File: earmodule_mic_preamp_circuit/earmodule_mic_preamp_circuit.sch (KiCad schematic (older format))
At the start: 29 parts

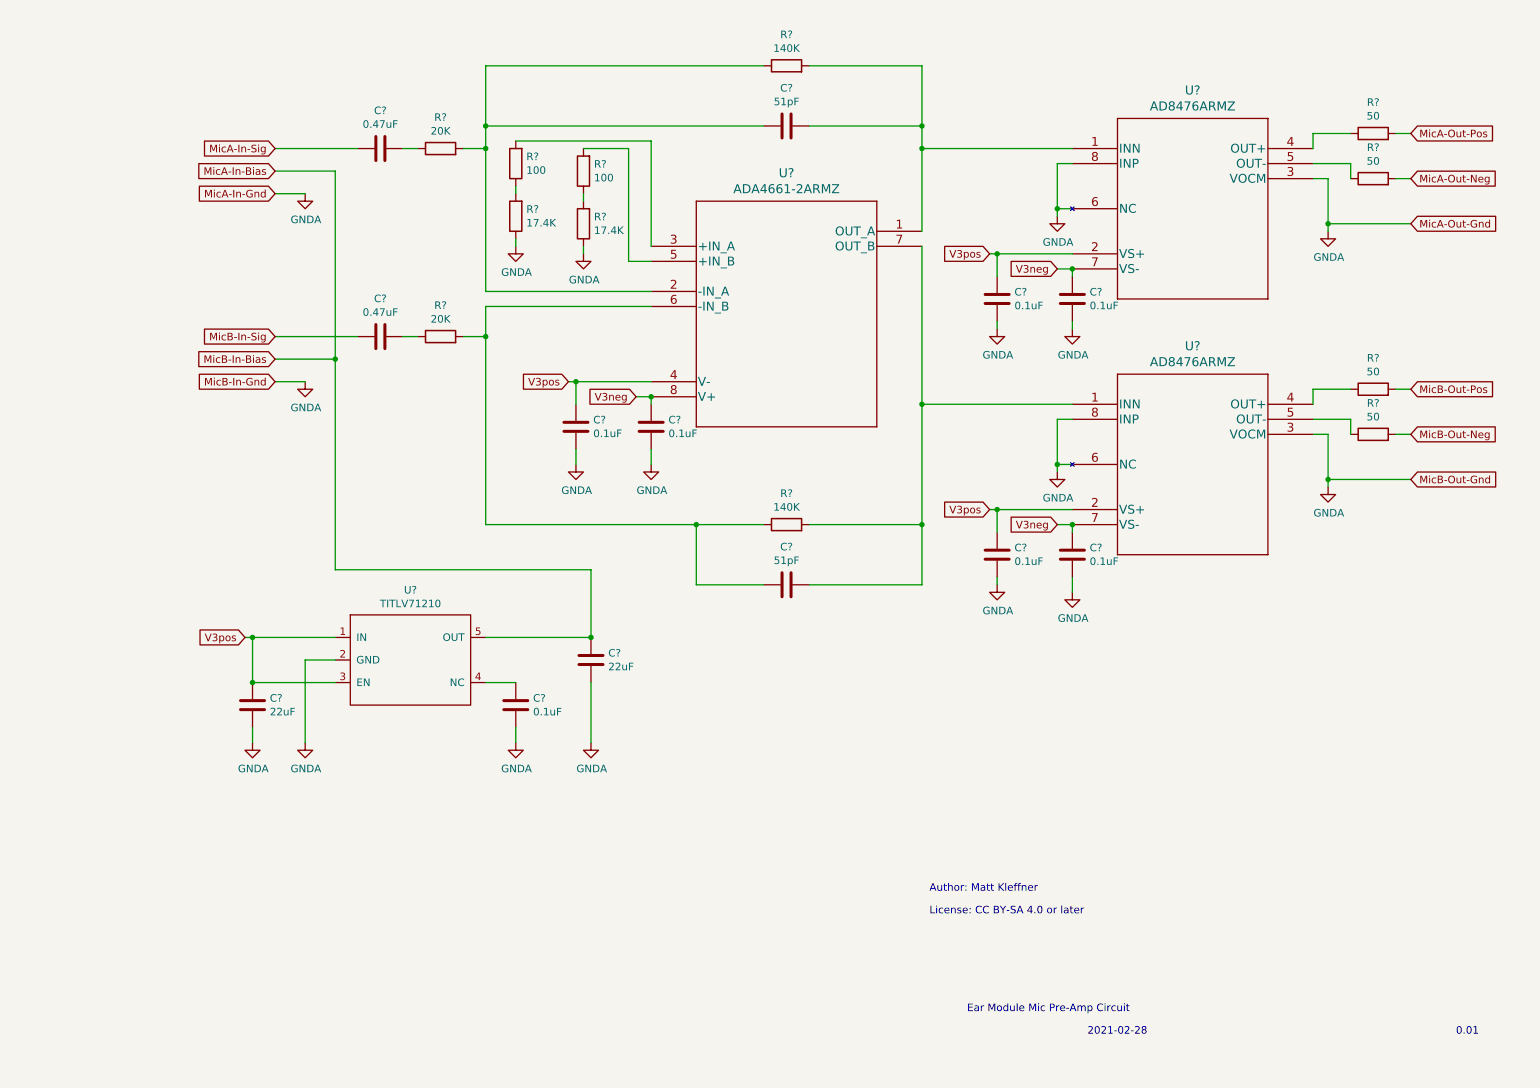
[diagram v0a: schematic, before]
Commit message: First complete PCB layout. Silkscreen needs to be fixed.
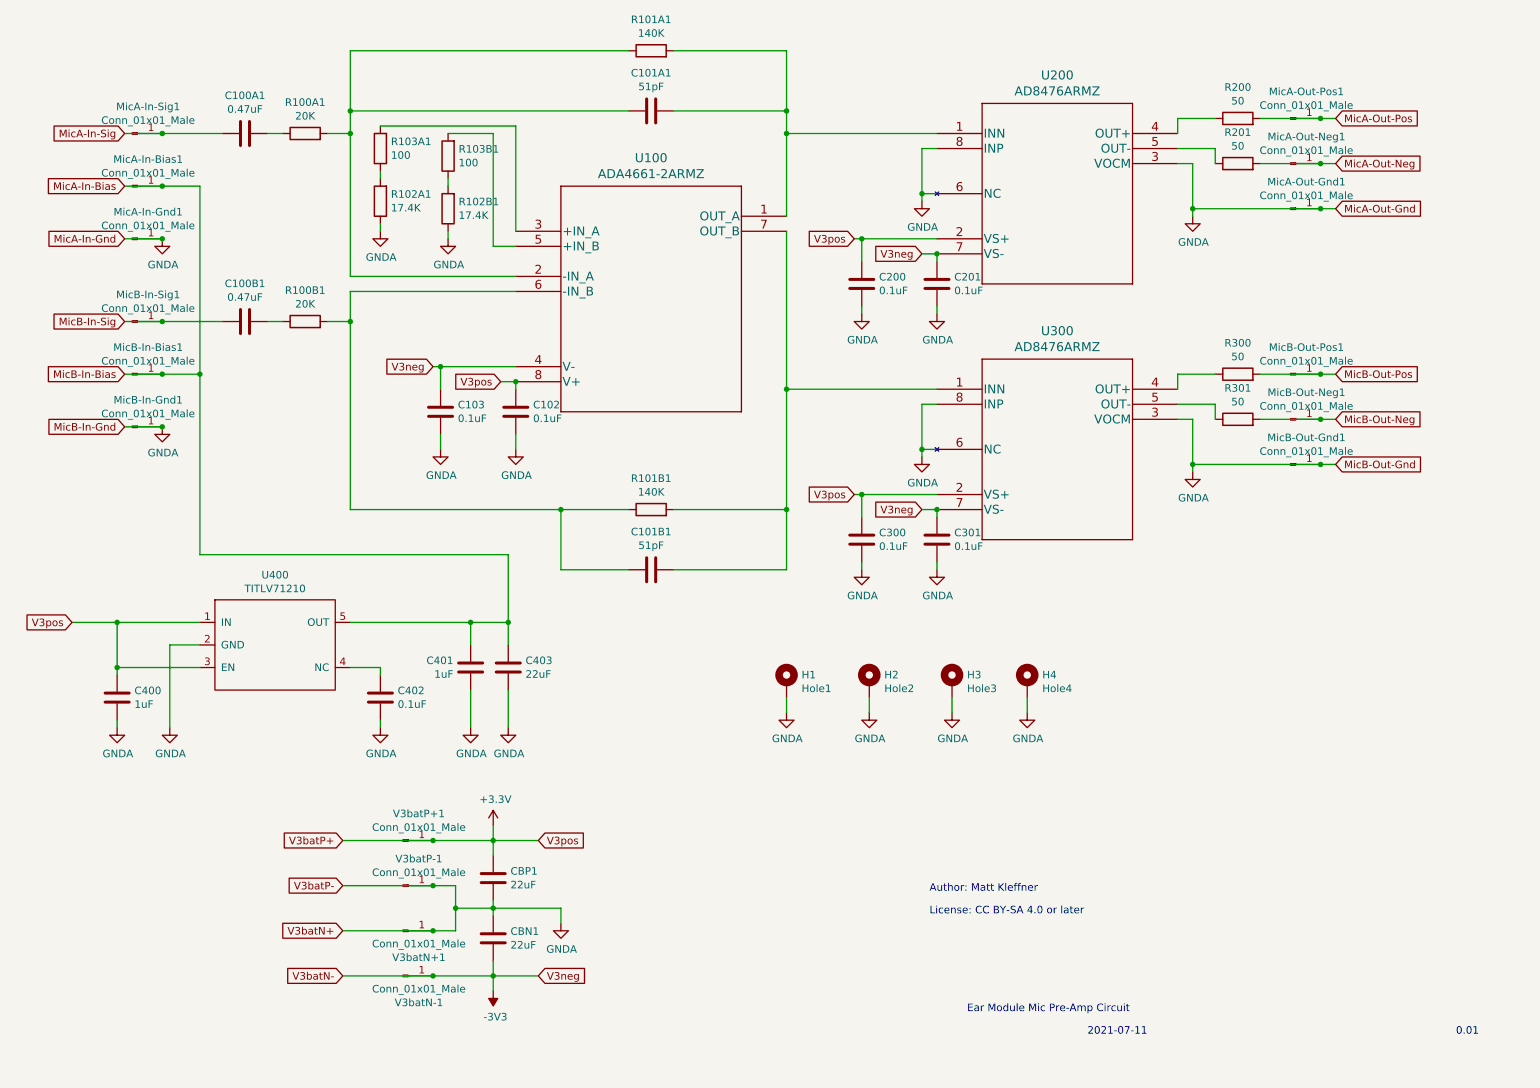
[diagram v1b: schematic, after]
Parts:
- added C400, C401: 1uF, Capacitor_SMD:C_0805_2012Metric_Pad1.15x1.40mm_HandSolder, symbol Device:C
- added CBN1: 22uF, Capacitor_SMD:C_1206_3216Metric_Pad1.42x1.75mm_HandSolder, symbol Device:C
- added H1: Hole1, MountingHole:MountingHole_2.7mm_M2.5_ISO7380, symbol Mechanical:MountingHole_Pad
- added H2: Hole2, MountingHole:MountingHole_2.7mm_M2.5_ISO7380, symbol Mechanical:MountingHole_Pad
- added H3: Hole3, MountingHole:MountingHole_2.7mm_M2.5_ISO7380, symbol Mechanical:MountingHole_Pad
- added H4: Hole4, MountingHole:MountingHole_2.7mm_M2.5_ISO7380, symbol Mechanical:MountingHole_Pad
- added MicA-In-Bias1, MicA-In-Gnd1, MicA-In-Sig1, MicA-Out-Gnd1, MicA-Out-Neg1, MicA-Out-Pos1, MicB-In-Bias1, MicB-In-Gnd1, MicB-In-Sig1, MicB-Out-Gnd1, MicB-Out-Neg1, MicB-Out-Pos1, V3batN+1, V3batN-1, V3batP+1, V3batP-1: Conn_01x01_Male, TestPoint:TestPoint_Pad_D2.0mm, symbol Connector:Conn_01x01_Male
- C100A1, C100B1, C101A1, C101B1, C102, C103, C200, C201, C300, C301, C402: renamed from C?; footprint (none) -> Capacitor_SMD:C_0402_1005Metric
- C403, CBP1: renamed from C?; footprint (none) -> Capacitor_SMD:C_1206_3216Metric_Pad1.42x1.75mm_HandSolder
- R100A1, R100B1, R101A1, R101B1, R102A1, R102B1, R103A1, R103B1, R200, R201, R300, R301: renamed from R?; footprint (none) -> Resistor_SMD:R_0402_1005Metric
- U100: renamed from U?; footprint RM_8_ADI -> footprints:ADA4661-2ARMZ
- U200, U300: renamed from U?; footprint RM_8_ADI -> footprints:AD8476ARMZ
- U400: renamed from U?; footprint (none) -> Package_TO_SOT_SMD:SOT-23-5_HandSoldering
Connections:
- net GNDA: now also C400.2, C401.2, CBN1.1, H1.1, H2.1, H3.1, H4.1, MicA-In-Gnd1.1 (Pin_1), MicA-Out-Gnd1.1 (Pin_1), MicB-In-Gnd1.1 (Pin_1), MicB-Out-Gnd1.1 (Pin_1), V3batN+1.1 (Pin_1), V3batP-1.1 (Pin_1)
- net MicA-In-Bias: now also C401.1, MicA-In-Bias1.1 (Pin_1), MicB-In-Bias1.1 (Pin_1)
- net MicA-In-Sig: now also MicA-In-Sig1.1 (Pin_1)
- net MicA-Out-Neg: now also MicA-Out-Neg1.1 (Pin_1)
- net MicA-Out-Pos: now also MicA-Out-Pos1.1 (Pin_1)
- net MicB-In-Sig: now also MicB-In-Sig1.1 (Pin_1)
- net MicB-Out-Neg: now also MicB-Out-Neg1.1 (Pin_1)
- net MicB-Out-Pos: now also MicB-Out-Pos1.1 (Pin_1)
- net V3neg renamed -3V3
- net -3V3: now also C103.1, U100.4 (V-), CBN1.2, V3batN-1.1 (Pin_1); no longer C102.1, U100.8 (V+)
- net V3pos renamed +3V3
- net +3V3: now also C102.1, U100.8 (V+), C400.1, V3batP+1.1 (Pin_1); no longer C103.1, U100.4 (V-)
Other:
- note added: "2021-07-11"
- note removed: "2021-02-28"
- moved on the sheet: C100A1, C100B1, C101A1, C101B1, C102, C103, C200, C201, C300, C301, C402, C403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

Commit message: Rearranged regulator layout for better co-location of parts. Cleaned up interface names.
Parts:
- renumbered MicA-In-Bias1 to MicInA-Bias1, MicA-In-Gnd1 to MicInA-Gnd1, MicA-In-Sig1 to MicInA-Sig1, MicB-In-Bias1 to MicInB-Bias1, MicB-In-Gnd1 to MicInB-Gnd1, MicB-In-Sig1 to MicInB-Sig1, MicA-Out-Gnd1 to MicOutA-Gnd1, MicA-Out-Neg1 to MicOutA-Neg1, MicA-Out-Pos1 to MicOutA-Pos1, MicB-Out-Gnd1 to MicOutB-Gnd1, MicB-Out-Neg1 to MicOutB-Neg1, MicB-Out-Pos1 to MicOutB-Pos1
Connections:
- net MicA-In-Bias renamed MicInA-Bias
- net MicA-In-Sig renamed MicInA-Sig
- net MicA-Out-Neg renamed MicOutA-Neg
- net MicA-Out-Pos renamed MicOutA-Pos
- net MicB-In-Sig renamed MicInB-Sig
- net MicB-Out-Neg renamed MicOutB-Neg
- net MicB-Out-Pos renamed MicOutB-Pos
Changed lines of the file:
@@
 	1800 1650 2050 1650
 $Comp
-L Connector:Conn_01x01_Male MicA-In-Sig1
+L Connector:Conn_01x01_Male MicInA-Sig1
 U 1 1 60ED7398
 P 1850 1650
-F 0 "MicA-In-Sig1" H 1956 1828 50  0000 C CNN
+F 0 "MicInA-Sig1" H 1956 1828 50  0000 C CNN
 F 1 "Conn_01x01_Male" H 1956 1737 50  0000 C CNN
 F 2 "TestPoint:TestPoint_Pad_D2.0mm" H 1850 1650 50  0001 C CNN
@@
 $EndComp
 $Comp
-L Connector:Conn_01x01_Male MicA-In-Bias1
+L Connector:Conn_01x01_Male MicInA-Bias1
 U 1 1 60EDA311
 P 1850 2000
-F 0 "MicA-In-Bias1" H 1956 2178 50  0000 C CNN
+F 0 "MicInA-Bias1" H 1956 2178 50  0000 C CNN
 F 1 "Conn_01x01_Male" H 1956 2087 50  0000 C CNN
 F 2 "TestPoint:TestPoint_Pad_D2.0mm" H 1850 2000 50  0001 C CNN
@@
 $EndComp
 $Comp
-L Connector:Conn_01x01_Male MicA-In-Gnd1
+L Connector:Conn_01x01_Male MicInA-Gnd1
 U 1 1 60EDDFEE
 P 1850 2350
-F 0 "MicA-In-Gnd1" H 1956 2528 50  0000 C CNN
+F 0 "MicInA-Gnd1" H 1956 2528 50  0000 C CNN
 F 1 "Conn_01x01_Male" H 1956 2437 50  0000 C CNN
 F 2 "TestPoint:TestPoint_Pad_D2.0mm" H 1850 2350 50  0001 C CNN
@@
 	2300 2000 2300 3250
 $Comp
-L Connector:Conn_01x01_Male MicB-In-Sig1
+L Connector:Conn_01x01_Male MicInB-Sig1
 U 1 1 60F3507A
 P 1850 2900
-F 0 "MicB-In-Sig1" H 1956 3078 50  0000 C CNN
+F 0 "MicInB-Sig1" H 1956 3078 50  0000 C CNN
 F 1 "Conn_01x01_Male" H 1956 2987 50  0000 C CNN
 F 2 "TestPoint:TestPoint_Pad_D2.0mm" H 1850 2900 50  0001 C CNN
@@
 $EndComp
 $Comp
-L Connector:Conn_01x01_Male MicB-In-Bias1
+L Connector:Conn_01x01_Male MicInB-Bias1
 U 1 1 60F390E4
 P 1850 3250
-F 0 "MicB-In-Bias1" H 1956 3428 50  0000 C CNN
+F 0 "MicInB-Bias1" H 1956 3428 50  0000 C CNN
 F 1 "Conn_01x01_Male" H 1956 3337 50  0000 C CNN
 F 2 "TestPoint:TestPoint_Pad_D2.0mm" H 1850 3250 50  0001 C CNN
@@
 $EndComp
 $Comp
-L Connector:Conn_01x01_Male MicB-In-Gnd1
+L Connector:Conn_01x01_Male MicInB-Gnd1
 U 1 1 60F3D199
 P 1850 3600
-F 0 "MicB-In-Gnd1" H 1956 3778 50  0000 C CNN
+F 0 "MicInB-Gnd1" H 1956 3778 50  0000 C CNN
 F 1 "Conn_01x01_Male" H 1956 3687 50  0000 C CNN
 F 2 "TestPoint:TestPoint_Pad_D2.0mm" H 1850 3600 50  0001 C CNN
@@
 	8900 2150 8900 2200
 $Comp
-L Connector:Conn_01x01_Male MicA-Out-Pos1
+L Connector:Conn_01x01_Male MicOutA-Pos1
 U 1 1 60FA54FA
 P 9550 1550
-F 0 "MicA-Out-Pos1" H 9656 1728 50  0000 C CNN
+F 0 "MicOutA-Pos1" H 9656 1728 50  0000 C CNN
 F 1 "Conn_01x01_Male" H 9656 1637 50  0000 C CNN
 F 2 "TestPoint:TestPoint_Pad_D2.0mm" H 9550 1550 50  0001 C CNN
@@
 	9350 1550 9750 1550
 $Comp
-L Connector:Conn_01x01_Male MicA-Out-Neg1
+L Connector:Conn_01x01_Male MicOutA-Neg1
 U 1 1 60FAAA8C
 P 9550 1850
-F 0 "MicA-Out-Neg1" H 9656 2028 50  0000 C CNN
+F 0 "MicOutA-Neg1" H 9656 2028 50  0000 C CNN
 F 1 "Conn_01x01_Male" H 9656 1937 50  0000 C CNN
 F 2 "TestPoint:TestPoint_Pad_D2.0mm" H 9550 1850 50  0001 C CNN
@@
 $EndComp
 $Comp
-L Connector:Conn_01x01_Male MicA-Out-Gnd1
+L Connector:Conn_01x01_Male MicOutA-Gnd1
 U 1 1 60FAEA59
 P 9550 2150
-F 0 "MicA-Out-Gnd1" H 9656 2328 50  0000 C CNN
+F 0 "MicOutA-Gnd1" H 9656 2328 50  0000 C CNN
 F 1 "Conn_01x01_Male" H 9656 2237 50  0000 C CNN
 F 2 "TestPoint:TestPoint_Pad_D2.0mm" H 9550 2150 50  0001 C CNN
@@
 	7200 2050 7100 2050
 $Comp
-L Connector:Conn_01x01_Male MicB-Out-Pos1
+L Connector:Conn_01x01_Male MicOutB-Pos1
 U 1 1 60FBFF69
 P 9550 3250
-F 0 "MicB-Out-Pos1" H 9656 3428 50  0000 C CNN
+F 0 "MicOutB-Pos1" H 9656 3428 50  0000 C CNN
 F 1 "Conn_01x01_Male" H 9656 3337 50  0000 C CNN
 F 2 "TestPoint:TestPoint_Pad_D2.0mm" H 9550 3250 50  0001 C CNN
@@
 	8900 3850 8900 3900
 $Comp
-L Connector:Conn_01x01_Male MicB-Out-Neg1
+L Connector:Conn_01x01_Male MicOutB-Neg1
 U 1 1 60FDC45F
 P 9550 3550
-F 0 "MicB-Out-Neg1" H 9656 3728 50  0000 C CNN
+F 0 "MicOutB-Neg1" H 9656 3728 50  0000 C CNN
 F 1 "Conn_01x01_Male" H 9656 3637 50  0000 C CNN
 F 2 "TestPoint:TestPoint_Pad_D2.0mm" H 9550 3550 50  0001 C CNN
@@
 	9750 3250 9850 3250
 $Comp
-L Connector:Conn_01x01_Male MicB-Out-Gnd1
+L Connector:Conn_01x01_Male MicOutB-Gnd1
 U 1 1 60FE4399
 P 9550 3850
-F 0 "MicB-Out-Gnd1" H 9656 4028 50  0000 C CNN
+F 0 "MicOutB-Gnd1" H 9656 4028 50  0000 C CNN
 F 1 "Conn_01x01_Male" H 9656 3937 50  0000 C CNN
 F 2 "TestPoint:TestPoint_Pad_D2.0mm" H 9550 3850 50  0001 C CNN
@@
 Wire Wire Line
 	4000 6650 3850 6650
-Wire Wire Line
-	3250 6950 3850 6950
-Wire Wire Line
-	3250 7250 3850 7250
-Connection ~ 3850 6350
-Wire Wire Line
-	3850 6350 3250 6350
 $Comp
 L Connector:Conn_01x01_Male V3batP-1
@@
 	1    0    0    1
 $EndComp
-Connection ~ 3850 6650
-Wire Wire Line
-	3850 6650 3250 6650
-Connection ~ 3850 7250
 Wire Wire Line
 	3850 6350 4250 6350
@@
 Text GLabel 4550 7250 2    50   Input ~ 0
 V3neg
-Connection ~ 3850 6950
 Wire Wire Line
 	3850 6950 4000 6950
@@
 Wire Wire Line
 	4250 7250 4550 7250
-Text GLabel 3250 7250 0    50   Input ~ 0
-V3batN-
-Text GLabel 3250 6950 0    50   Input ~ 0
-V3batN+
-Text GLabel 3250 6650 0    50   Input ~ 0
-V3batP-
-Text GLabel 3250 6350 0    50   Input ~ 0
-V3batP+
 Text GLabel 9850 3250 2    50   Input ~ 0
-MicB-Out-Pos
+MicOutB-Pos
 Text GLabel 9850 3550 2    50   Input ~ 0
-MicB-Out-Neg
+MicOutB-Neg
 Text GLabel 9850 3850 2    50   Input ~ 0
-MicB-Out-Gnd
+MicOutB-Gnd
 Text GLabel 9850 1550 2    50   Input ~ 0
-MicA-Out-Pos
+MicOutA-Pos
 Text GLabel 9850 1850 2    50   Input ~ 0
-MicA-Out-Neg
+MicOutA-Neg
 Text GLabel 9850 2150 2    50   Input ~ 0
-MicA-Out-Gnd
+MicOutA-Gnd
 Text GLabel 1800 1650 0    50   Input ~ 0
-MicA-In-Sig
+MicInA-Sig
 Text GLabel 1800 2900 0    50   Input ~ 0
-MicB-In-Sig
+MicInB-Sig
 Text GLabel 1800 3600 0    50   Input ~ 0
-MicB-In-Gnd
+MicInB-Gnd
 Text GLabel 1800 2350 0    50   Input ~ 0
-MicA-In-Gnd
+MicInA-Gnd
 Text GLabel 1800 3250 0    50   Input ~ 0
-MicB-In-Bias
+MicInB-Bias
 Text GLabel 1800 2000 0    50   Input ~ 0
-MicA-In-Bias
+MicInA-Bias
 $Comp
 L Mechanical:MountingHole_Pad H1

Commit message: Enlarged board and wire solder pad sizes. Added small decoupling caps in bias circuit. Finalized naming, numbering, and placement of text.
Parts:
- removed H1: Hole1, MountingHole:MountingHole_2.7mm_M2.5_ISO7380, symbol Mechanical:MountingHole_Pad
- removed H2: Hole2, MountingHole:MountingHole_2.7mm_M2.5_ISO7380, symbol Mechanical:MountingHole_Pad
- removed H3: Hole3, MountingHole:MountingHole_2.7mm_M2.5_ISO7380, symbol Mechanical:MountingHole_Pad
- removed H4: Hole4, MountingHole:MountingHole_2.7mm_M2.5_ISO7380, symbol Mechanical:MountingHole_Pad
- added C401: 0.1uF, Capacitor_SMD:C_0402_1005Metric, symbol Device:C
- added H1, H2, H3, H4: MountingHole, MountingHole:MountingHole_2.7mm_M2.5_ISO7380, symbol Mechanical:MountingHole
- MicIn-Bias1: renamed from MicInA-Bias1; footprint TestPoint:TestPoint_Pad_D2.0mm -> TestPoint:TestPoint_Pad_D4.0mm
- MicIn-Bias2: renamed from MicInB-Bias1; footprint TestPoint:TestPoint_Pad_D2.0mm -> TestPoint:TestPoint_Pad_D4.0mm
- MicIn-Gnd1: renamed from MicInA-Gnd1; footprint TestPoint:TestPoint_Pad_D2.0mm -> TestPoint:TestPoint_Pad_D4.0mm
- MicIn-Gnd2: renamed from MicInB-Gnd1; footprint TestPoint:TestPoint_Pad_D2.0mm -> TestPoint:TestPoint_Pad_D4.0mm
- MicIn-Sig1: renamed from MicInA-Sig1; footprint TestPoint:TestPoint_Pad_D2.0mm -> TestPoint:TestPoint_Pad_D4.0mm
- MicIn-Sig2: renamed from MicInB-Sig1; footprint TestPoint:TestPoint_Pad_D2.0mm -> TestPoint:TestPoint_Pad_D4.0mm
- MicOut-Gnd1: renamed from MicOutA-Gnd1; footprint TestPoint:TestPoint_Pad_D2.0mm -> TestPoint:TestPoint_Pad_D4.0mm
- MicOut-Gnd2: renamed from MicOutB-Gnd1; footprint TestPoint:TestPoint_Pad_D2.0mm -> TestPoint:TestPoint_Pad_D4.0mm
- MicOut-Neg1: renamed from MicOutA-Neg1; footprint TestPoint:TestPoint_Pad_D2.0mm -> TestPoint:TestPoint_Pad_D4.0mm
- MicOut-Neg2: renamed from MicOutB-Neg1; footprint TestPoint:TestPoint_Pad_D2.0mm -> TestPoint:TestPoint_Pad_D4.0mm
- MicOut-Pos1: renamed from MicOutA-Pos1; footprint TestPoint:TestPoint_Pad_D2.0mm -> TestPoint:TestPoint_Pad_D4.0mm
- MicOut-Pos2: renamed from MicOutB-Pos1; footprint TestPoint:TestPoint_Pad_D2.0mm -> TestPoint:TestPoint_Pad_D4.0mm
- Ns_T+_V3: renamed from V3batN+1; footprint TestPoint:TestPoint_Pad_D2.0mm -> TestPoint:TestPoint_Pad_D4.0mm
- Ns_T-_V3: renamed from V3batN-1; footprint TestPoint:TestPoint_Pad_D2.0mm -> TestPoint:TestPoint_Pad_D4.0mm
- Ps_T+_V3: renamed from V3batP+1; footprint TestPoint:TestPoint_Pad_D2.0mm -> TestPoint:TestPoint_Pad_D4.0mm
- Ps_T-_V3: renamed from V3batP-1; footprint TestPoint:TestPoint_Pad_D2.0mm -> TestPoint:TestPoint_Pad_D4.0mm
- renumbered C200 to C100, C201 to C101, C300 to C200, C301 to C201, C100A1 to C301, C100B1 to C302, C102 to C303, C103 to C304, C101A1 to C311, C101B1 to C312, C401 to C403, C403 to C404, CBN1 to CN1, CBP1 to CP1, R200 to R100, R201 to R101, R300 to R200, R301 to R201, R100A1 to R301, R100B1 to R302, R101A1 to R311, R101B1 to R312, R102A1 to R321, R102B1 to R322, R103A1 to R331, R103B1 to R332, U200 to U100, U300 to U200, U100 to U300
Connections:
- net MicInA-Bias is gone; now on an unnamed net: C403.1, C404.1, MicIn-Bias1.1 (Pin_1), MicIn-Bias2.1 (Pin_1), U400.5 (OUT)
- net +3V3: now also C401.1
- net GNDA: now also U400.4 (NC), C401.2
- net at C402.1: no longer U400.4 (NC)
- net MicInA-Sig: no longer names the net of C301.2, MicIn-Sig1.1 (Pin_1)
- net MicInB-Sig: no longer names the net of C302.2, MicIn-Sig2.1 (Pin_1)
- net MicOutA-Neg: no longer names the net of MicOut-Neg1.1 (Pin_1), R101.2
- net MicOutA-Pos: no longer names the net of MicOut-Pos1.1 (Pin_1), R100.2
- net MicOutB-Neg: no longer names the net of MicOut-Neg2.1 (Pin_1), R201.2
- net MicOutB-Pos: no longer names the net of MicOut-Pos2.1 (Pin_1), R200.2
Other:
- note removed: "0.01"
- note removed: "2021-07-11"
- note removed: "Ear Module Mic Pre-Amp Circuit"
- note removed: "License: CC BY-SA 4.0 or later"
- moved on the sheet: C400, C403, C404
